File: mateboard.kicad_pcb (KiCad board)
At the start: 6 copper layers, 70 x 50 mm, 179 parts, among them IC1 OSD335x, IC2 SN74LVC2G241DCUR, IC3 NAND_4GB, IC4 WL1835MODGBMOCT, J1 IO1, J10 TEST_1P, J11 TEST_1P, J12 ANT2, J13 TEST_1P, J14 TEST_1P, J15 VDDS_PLL, J16 VDDS_DDR, J17 VDD_MPU, J18 VDD_CORE, J19 VDD_3V3AUX, J2 IO2, J3 GS2, J4 ANT2, J5 TEST_1P, J6 TEST_1P, J7 TEST_1P, J8 TEST_1P, J9 TEST_1P, Q1 BSS138, Q2 BSS138, U1 AP2112K-3.3TRG1, U10 TXS0108, U11 TXS0108, U2 AP2112K-1.8TRG1, U3 TL1963A-33DCQR, U4 24LC32AT-I, U5 TPS2065CDGN, U6 TPD4S012, U7 TPD4S012, U8 SN74LVC1G06DCK, U9 74LVC1G07DCK, X1 NZ2520SB-32.768KHZ-NSA3534C, Y1 24MHz, Y2 32.768kHz

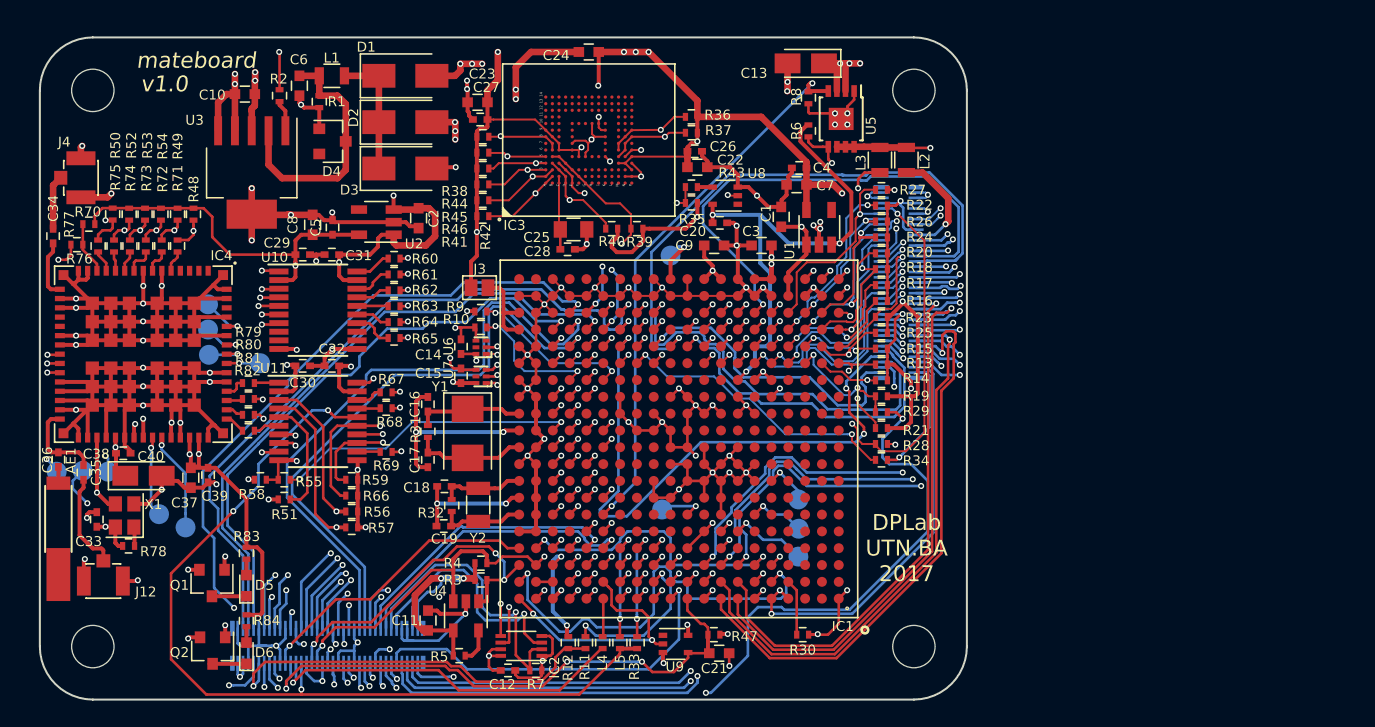
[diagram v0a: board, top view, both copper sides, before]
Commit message: add clamping protection for 3v3a and 3v3b
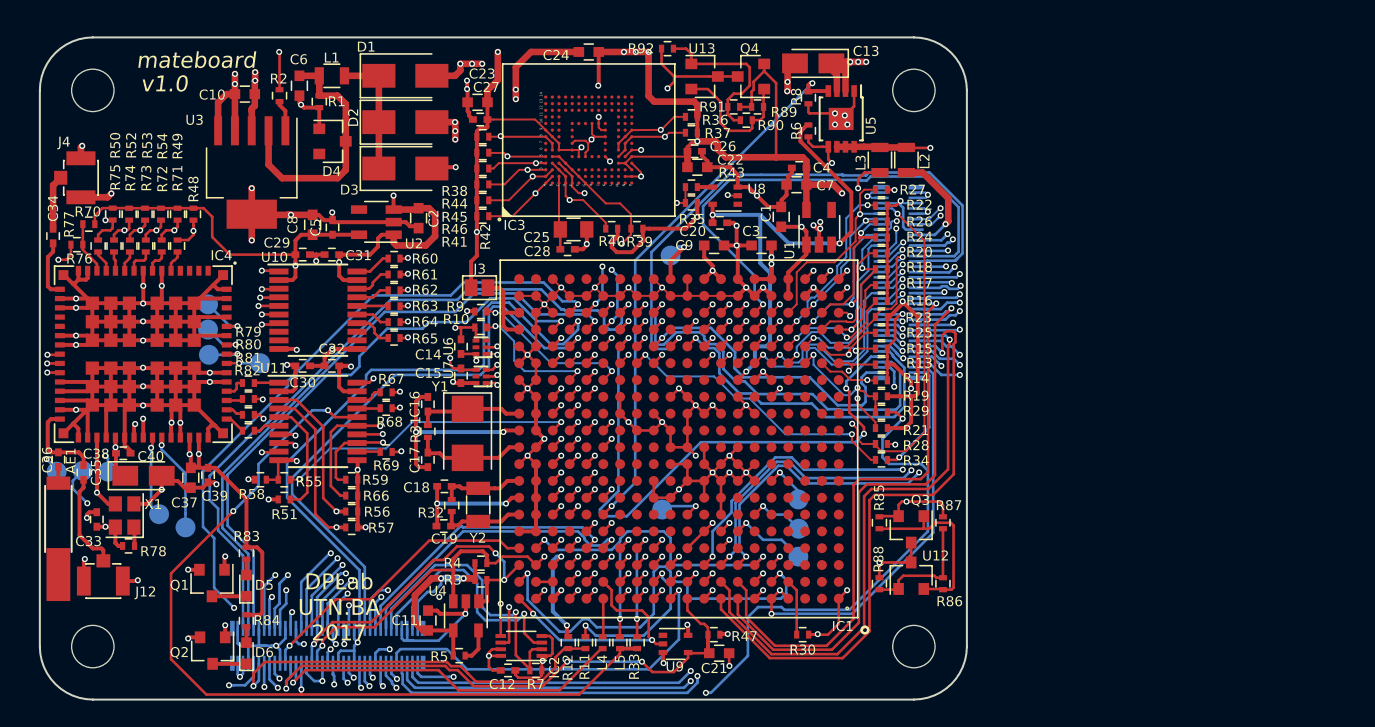
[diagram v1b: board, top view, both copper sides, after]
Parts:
- added Q3: MMBT2907, TO_SOT_Packages_SMD:SOT-23, F.Cu at (156.6, 145.9)
- added Q4: MMBT2907, TO_SOT_Packages_SMD:SOT-23, F.Cu at (144.5, 111.7)
- added R85: 499, Resistors_SMD:R_0402, F.Cu at (154.2, 145.4)
- added R86: DNP, Resistors_SMD:R_0402, F.Cu at (159.0, 150.0)
- added R87: 10k, Resistors_SMD:R_0402, F.Cu at (159.0, 145.4)
- added R88: 40.2k, Resistors_SMD:R_0402, F.Cu at (154.2, 150.0)
- added R89: 499, Resistors_SMD:R_0402, F.Cu at (145.0, 114.0)
- added R90: DNP, Resistors_SMD:R_0402, F.Cu at (144.2, 115.0)
- added R91: 10k, Resistors_SMD:R_0402, F.Cu at (143.2, 114.0)
- added R92: 40.2k, Resistors_SMD:R_0402, F.Cu at (138.2, 109.6)
- added U12: TLVH431, TO_SOT_Packages_SMD:SOT-23, F.Cu at (156.6, 149.4)
- added U13: TLVH431, TO_SOT_Packages_SMD:SOT-23, F.Cu at (141.0, 111.7)
- moved C13 0.56 mm to (149.2, 110.7)
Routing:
- net VDD_1V8: track 31.4 -> 101.3 mm, vias 4 -> 6
- net VDD_3V3A: track 66.9 -> 82.5 mm, vias 6 -> 7
- net Net-(Q3-Pad1): track 0.00 -> 13.9 mm
- net VDD_3V3B: track 238.2 -> 250.9 mm
- net Net-(R90-Pad1): track 0.00 -> 12.5 mm
- net Net-(Q4-Pad1): track 0.00 -> 10.6 mm
- net Net-(R86-Pad1): track 0.00 -> 9.38 mm
- net SYS_5V: track 147.4 -> 142.8 mm
- net /AIN6: track 44.0 -> 46.9 mm
- net /AIN5: track 41.8 -> 44.5 mm
- net /AIN2: track 40.9 -> 43.4 mm
- net /AIN7: track 36.2 -> 33.9 mm
- net /AIN3: track 42.3 -> 44.4 mm
- net /GPIO1_14: track 69.9 -> 68.7 mm
- net /AIN1: track 38.6 -> 37.7 mm
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
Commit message: footprints updated, add power led
Signed-off-by: Pablo Ridolfi <pabloridolfi@outlook.com>
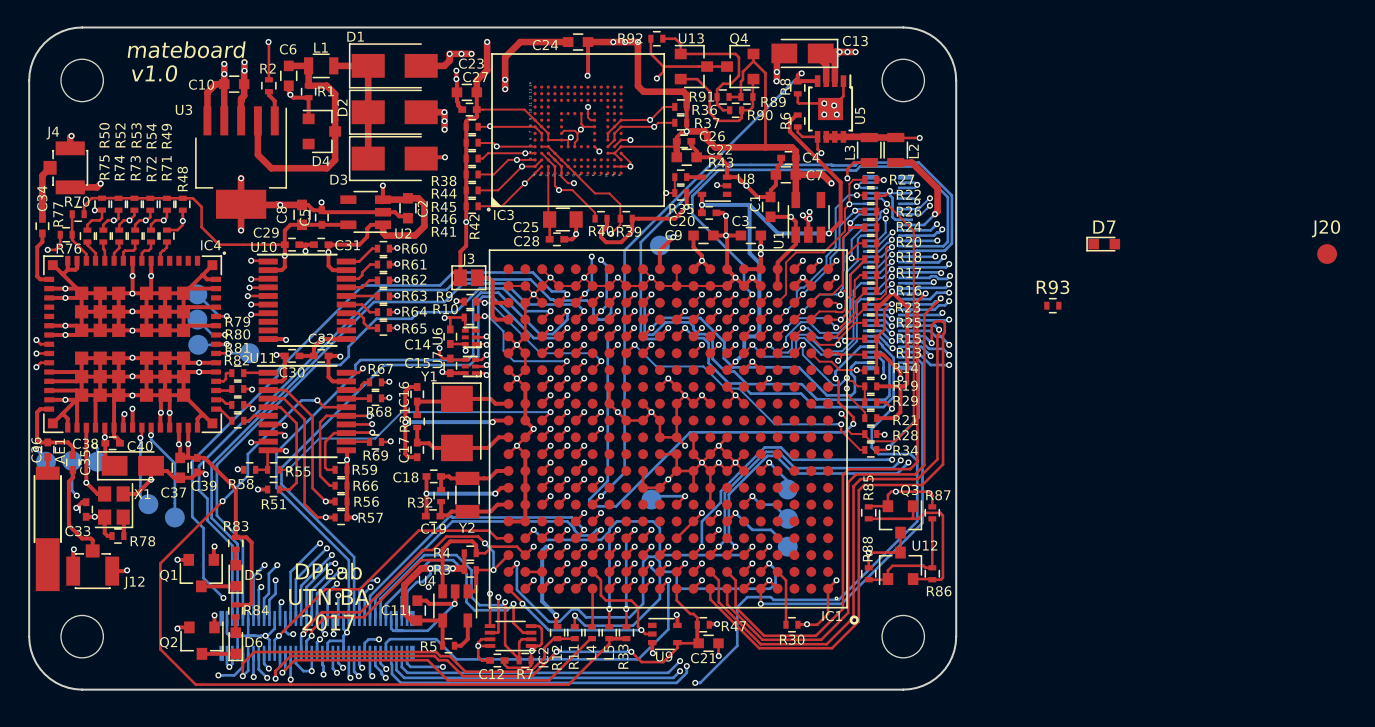
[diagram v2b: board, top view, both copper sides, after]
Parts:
- added D7: LTST-C191TBKT, LEDs:LED_0603, F.Cu at (171.2, 124.4)
- added J20: VDD_RTC, Measurement_Points:Measurement_Point_Round-SMD-Pad_Small, F.Cu at (188.0, 125.1)
- added R93: 4.75k, Resistors_SMD:R_0402, F.Cu at (167.3, 129.0)
- moved C1 1.10 mm to (146.0, 121.5)
- moved C10 1.10 mm to (105.5, 112.3)
- moved C12 1.10 mm to (125.3, 155.8)
- moved C14 1.10 mm to (121.8, 131.3)
- moved C15 1.10 mm to (121.8, 133.6)
- moved C16 1.10 mm to (119.3, 135.7)
- moved C17 1.10 mm to (119.3, 139.9)
- moved C18 1.10 mm to (120.5, 141.9)
- moved C19 1.10 mm to (120.5, 144.9)
- moved C2 1.10 mm to (118.6, 121.7)
- moved C20 1.10 mm to (141.3, 122.0)
- moved C22 1.10 mm to (139.7, 117.8)
- moved C23 1.10 mm to (123.0, 112.9)
- moved C24 1.10 mm to (131.4, 109.1)
- moved C26 1.10 mm to (139.4, 116.6)
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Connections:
- net Net-(IC1-PadY11) renamed /Power Management/VDD_3V3AUX
- IC1 pad N6: VRTC -> /CPU Power/VDD_RTC
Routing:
- net /Wi-Fi BLE/WL_SDIO_D3: track 18.8 -> 19.4 mm
- net Net-(IC4-Pad25): track 11.0 -> 11.5 mm
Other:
- net class Default: clearance 0.1 -> 0.15
- rule trace_clearance: 0.1 -> 0.15

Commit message: fixing design
Signed-off-by: Pablo Ridolfi <pabloridolfi@outlook.com>
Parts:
- removed C14, C15: 100nF/6.3V, Capacitors_SMD:C_0402
- removed U6, U7: TPD4S012, footprints:SON-6
- J20: moved to B.Cu
- MH1, MH2, MH3, MH4: renamed from REF**; value MountingHole_3.2mm_M3 -> Mounting hole
- moved J20 47.8 mm to (141.8, 137.3)
- moved D7 33.7 mm to (137.5, 122.6), turned to 180 degrees
- moved R93 30.7 mm to (137.0, 124.0), turned to 180 degrees
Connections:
- MH1 pad 1: (no net) -> Net-(MH1-Pad1)
- MH2 pad 1: (no net) -> Net-(MH2-Pad1)
- MH3 pad 1: (no net) -> Net-(MH3-Pad1)
- MH4 pad 1: (no net) -> Net-(MH4-Pad1)
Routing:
- net /CPU Power/VDD_RTC: track 0.00 -> 5.07 mm, vias 0 -> 1
- net (no net): track 0.00 -> 2.60 mm, vias 0 -> 1
- net GNDD: track 446.5 -> 448.8 mm, vias 102 -> 100
- net Net-(D7-Pad2): track 0.00 -> 1.46 mm
- net /Power Management/VDD_3V3AUX: track 4.11 -> 5.27 mm

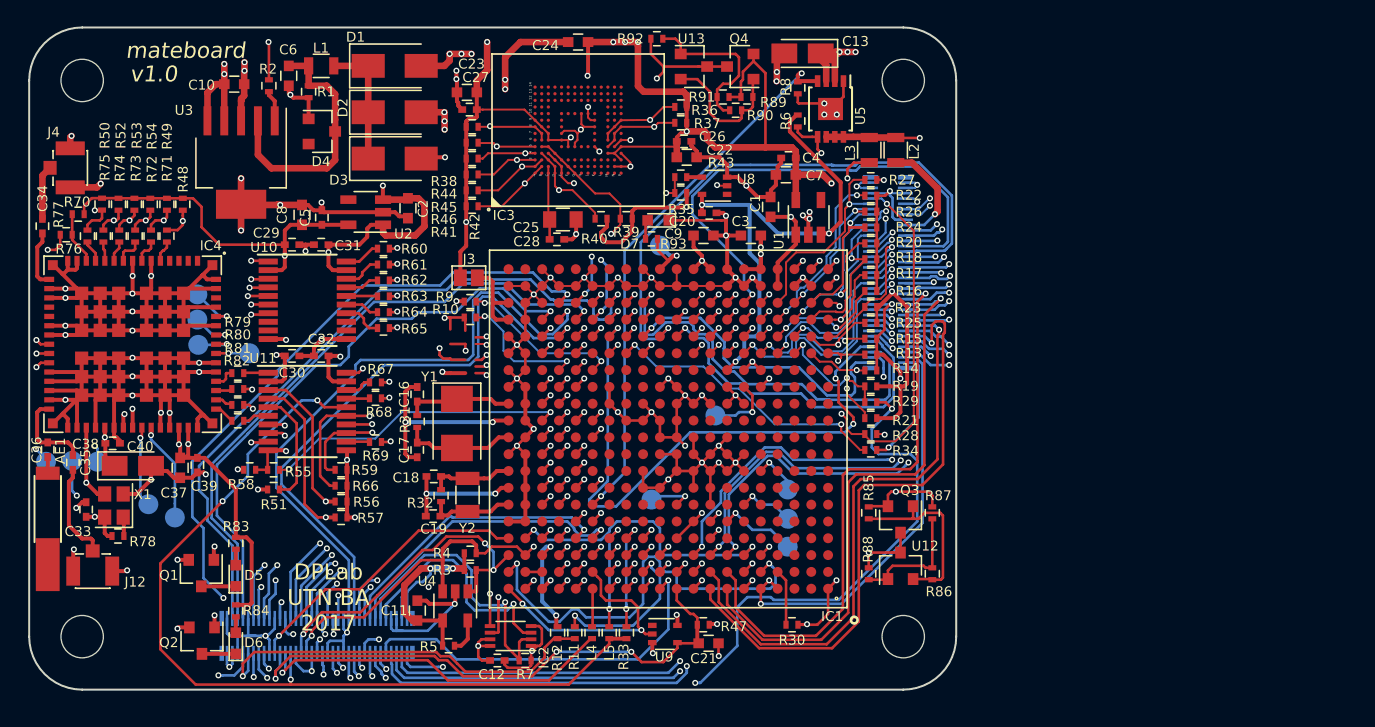
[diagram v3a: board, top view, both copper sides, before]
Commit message: j1 and j2 aligned, 3d model test
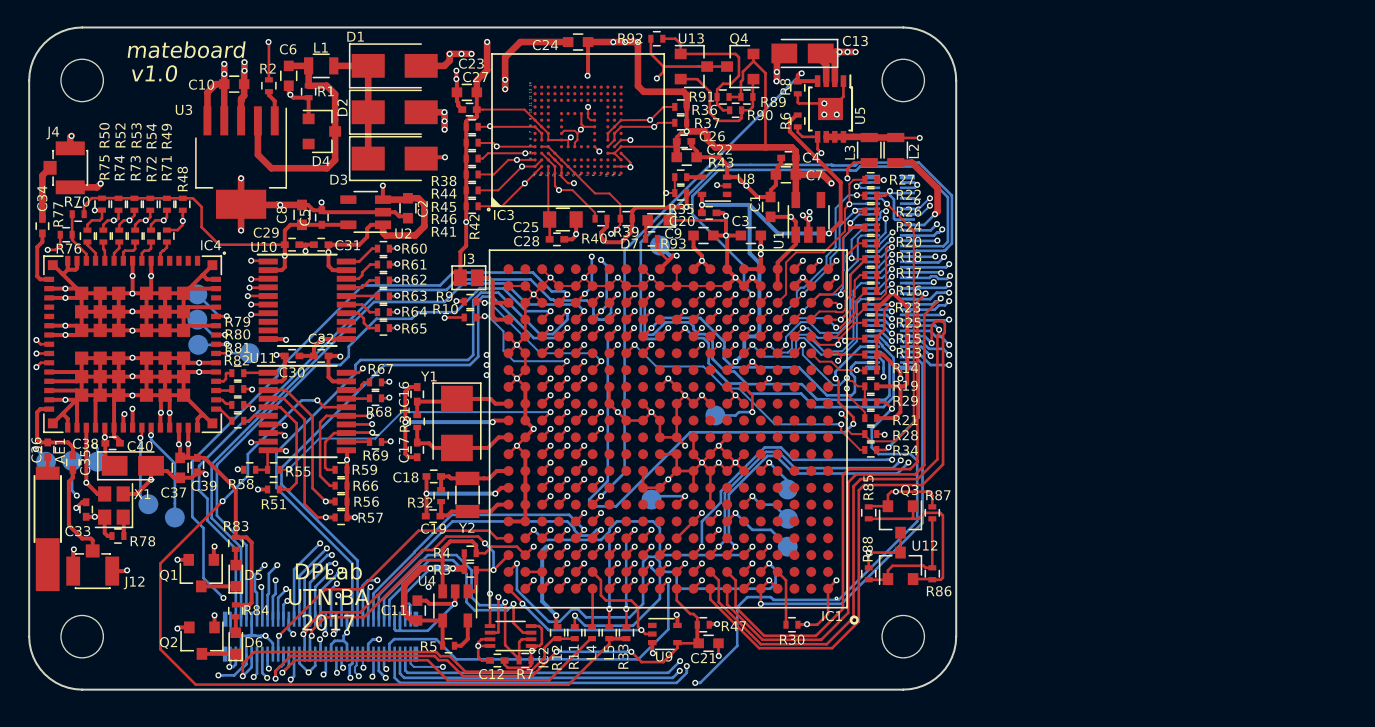
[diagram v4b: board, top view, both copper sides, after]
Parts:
- moved J2 0.27 mm to (112.0, 154.0)
- moved J1 0.15 mm to (155.0, 126.5)
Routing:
- net /USB-UART-WL-BT-GPIO/USB1_PWR: track 56.6 -> 48.9 mm, vias 2 -> 1
- net GNDD: track 448.8 -> 445.9 mm, vias 100 -> 101
- net USB_DC: track 73.5 -> 70.7 mm, vias 5 -> 4
- net (no net): track 2.60 -> 0.00 mm, vias 1 -> 0
- net /USB1_DM: track 57.5 -> 56.1 mm, vias 3 -> 2
- net /USB0_ID: track 36.6 -> 35.5 mm
- net /USB1_DP: track 61.7 -> 60.6 mm, vias 3 -> 2
- net /USB0_DP: track 35.8 -> 34.9 mm
- net VDD_3V3B: track 251.2 -> 250.4 mm
- net /USB0_DM: track 32.3 -> 31.6 mm

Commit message: mateboard v1.0
Signed-off-by: Pablo Ridolfi <pabloridolfi@outlook.com>
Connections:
- net /USB0_DM renamed /USB0_D-
- net /USB0_DP renamed /USB0_D+
- net /USB1_DM renamed /USB1_D-
- net /USB1_DP renamed /USB1_D+
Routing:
- net GNDD: track 445.9 -> 479.5 mm, vias 101 -> 102
- net /USB1_D+: track 60.6 -> 48.2 mm
- net /USB0_D-: track 31.6 -> 40.8 mm, vias 3 -> 2
- net /USB1_D-: track 56.1 -> 47.9 mm
- net /USB0_D+: track 34.9 -> 42.7 mm, vias 3 -> 2
- net /PWR_BUT: track 22.3 -> 24.9 mm
- net /VBAT_TEMP: track 12.4 -> 13.5 mm
- net /USB0_ID: track 35.5 -> 36.4 mm
- net /VBAT_SENSE: track 12.1 -> 13.0 mm
- net /CLKOUT2: track 67.2 -> 68.0 mm
- net VDD_3V3B: track 250.4 -> 251.2 mm
- net GNDA: track 71.9 -> 71.2 mm
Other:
- net class Default: clearance 0.15 -> 0.1
- rule trace_clearance: 0.15 -> 0.1

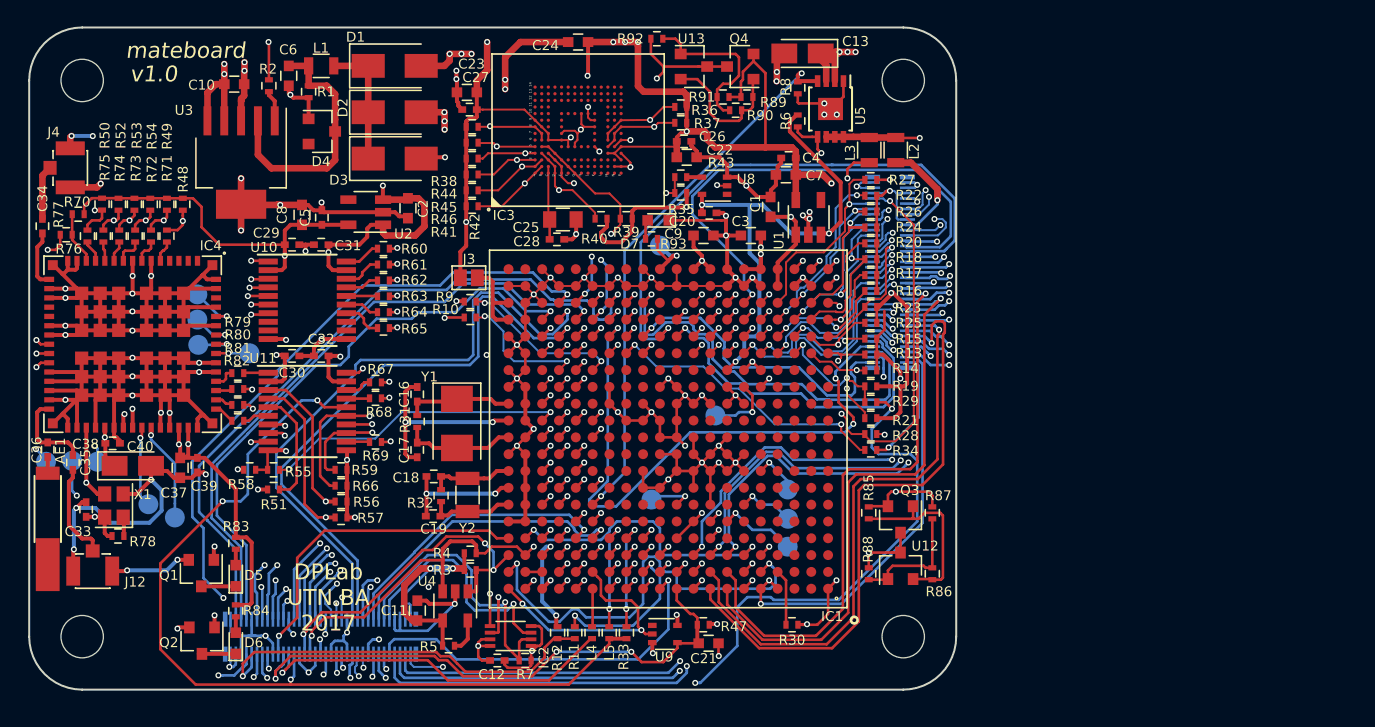
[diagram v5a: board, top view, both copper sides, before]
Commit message: gerbers updated, bom using kicost
Signed-off-by: Pablo Ridolfi <pabloridolfi@outlook.com>
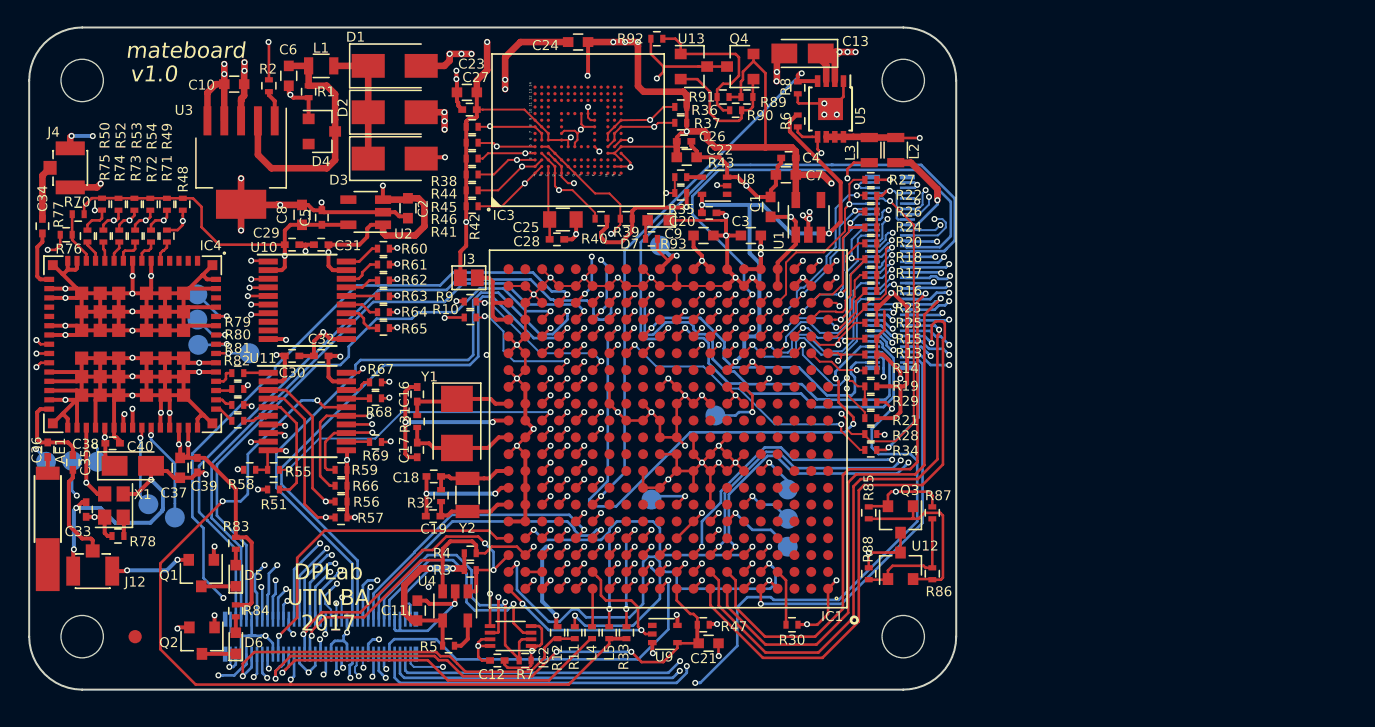
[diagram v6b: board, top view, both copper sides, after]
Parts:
- added REF**: Fiducial_1mm_Dia_2.54mm_Outer_CopperTop, Fiducials:Fiducial_1mm_Dia_2.54mm_Outer_CopperTop, F.Cu at (98.0, 154.0)
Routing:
- net /AIN6: track 46.9 -> 47.7 mm
- net GNDD: track 479.5 -> 480.3 mm
- net /AIN5: track 44.5 -> 45.1 mm
- net VDD_3V3_WIFI: track 97.6 -> 97.1 mm
